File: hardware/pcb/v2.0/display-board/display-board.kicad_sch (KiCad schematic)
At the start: 53 parts, among them J1 Conn_01x01_Socket, J2 Conn_01x01_Socket, J3 Conn_01x01_Socket, J4 Conn_01x01_Socket, J5 Conn_01x01_Socket, J6 Conn_01x01_Socket, Q1 AO3400A, Q2 AO3401A, Q3 AO3400A, Q4 AO3401A, Q5 AO3400A, Q6 AO3401A, Q7 AO3400A, SW1 SW_Push, SW2 SW_Push, U1 TLC5940PWP, U2 7Seg 2Dig 0.56in, U3 GS-S2011AB, U4 7Seg 2Dig 0.56in, U5 GS-S2011AB

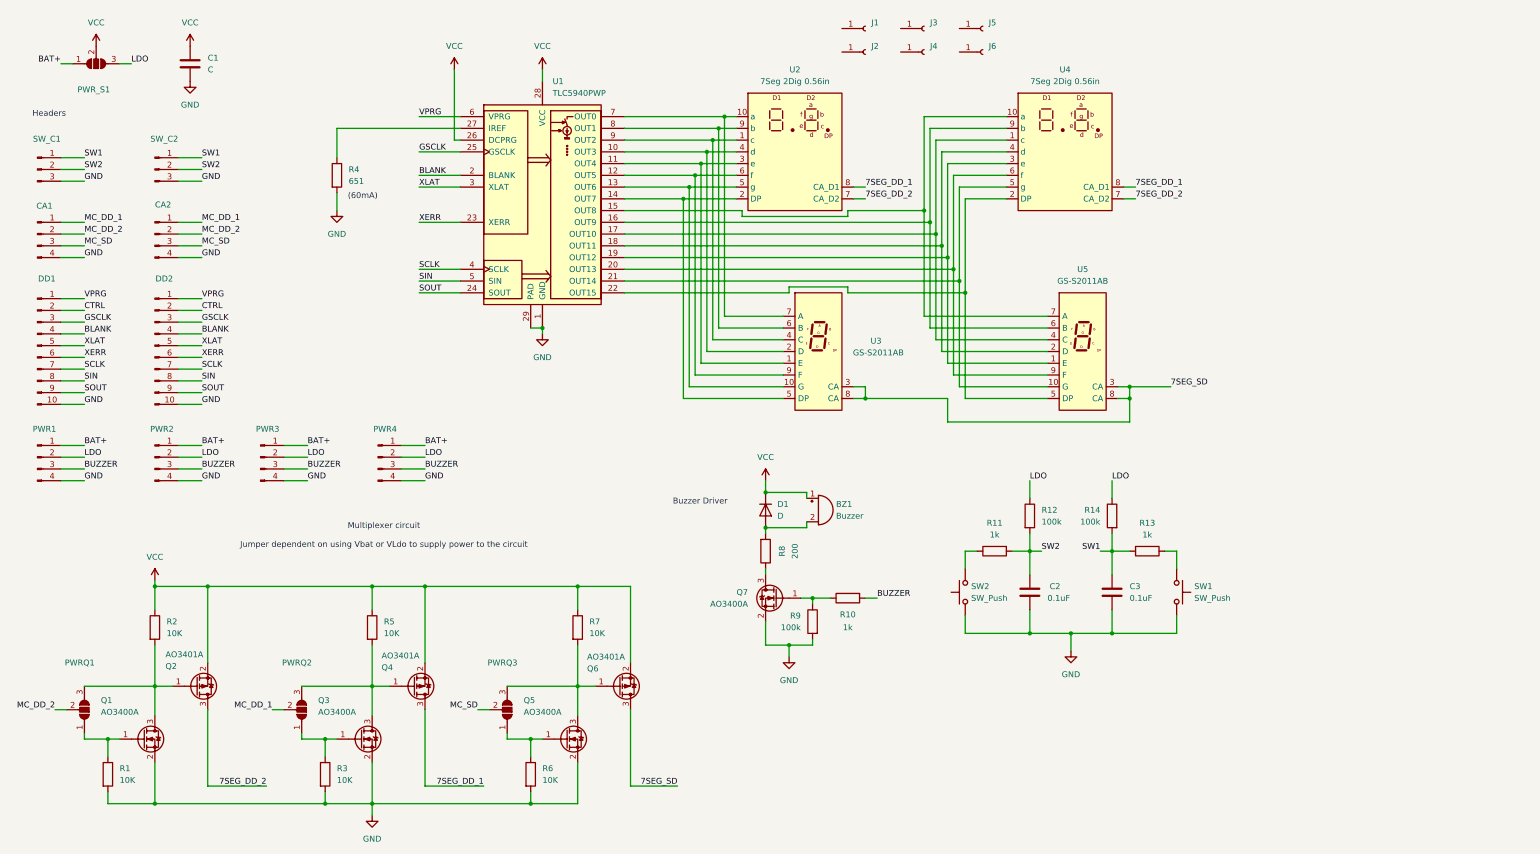
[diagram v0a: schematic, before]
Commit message: v2.0 of the main and display board is ready and in production
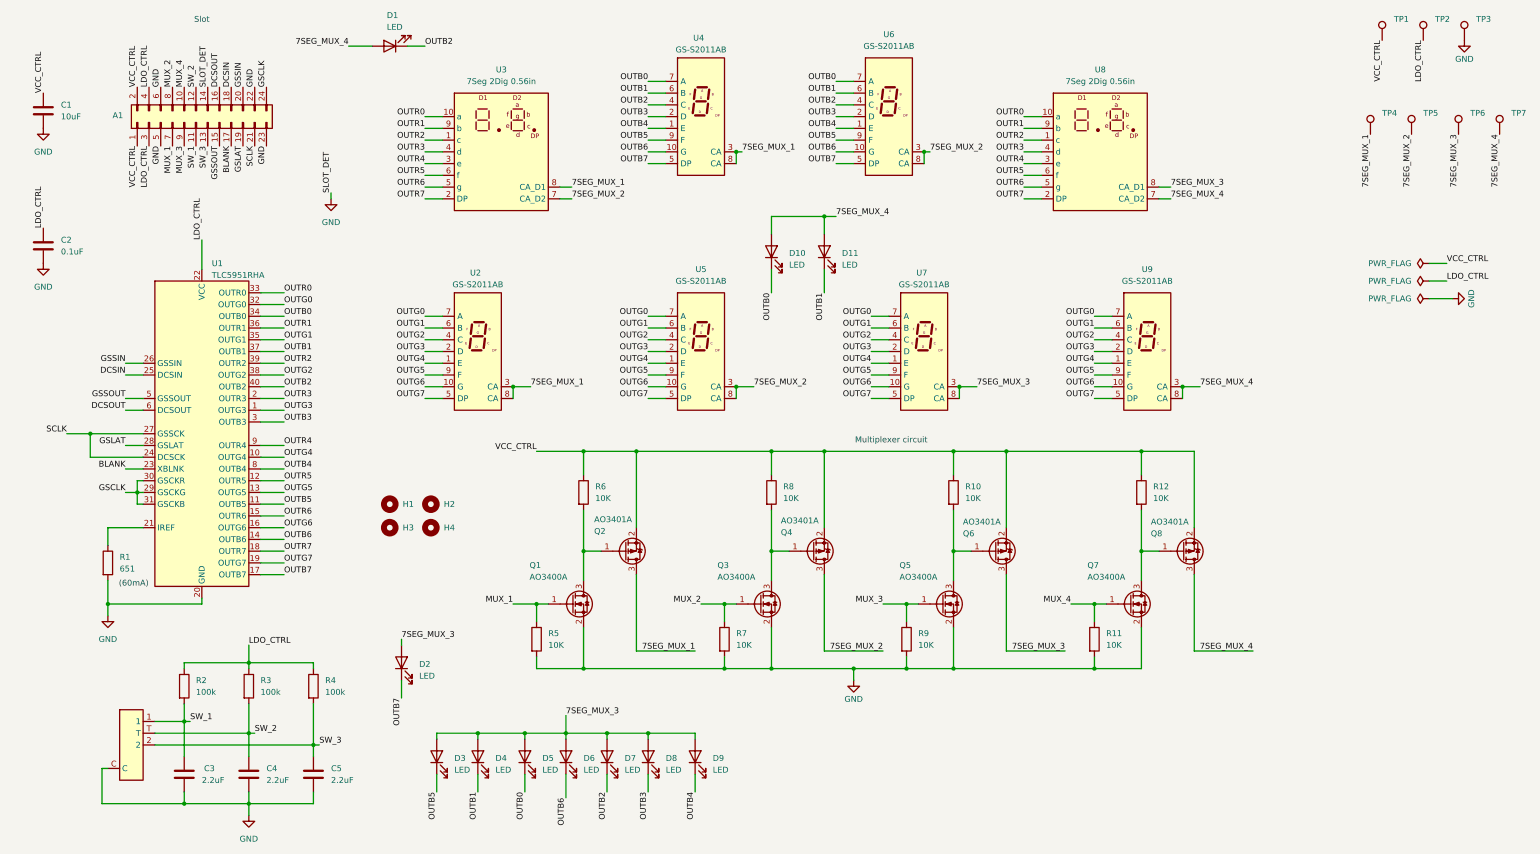
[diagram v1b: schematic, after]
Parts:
- removed BZ1: Buzzer, Buzzer_Beeper:Buzzer_TDK_PS1240P02BT_D12.2mm_H6.5mm, symbol Device:Buzzer
- removed CA1, CA2, PWR1, PWR2, PWR3, PWR4: Conn_01x04_Pin, Connector_PinHeader_1.27mm:PinHeader_1x04_P1.27mm_Vertical, symbol Connector:Conn_01x04_Pin
- removed D1: D, Diode_SMD:D_SOD-323_HandSoldering, symbol Device:D
- removed DD1, DD2: Conn_01x10_Pin, Connector_PinSocket_1.27mm:PinSocket_1x10_P1.27mm_Vertical, symbol Connector:Conn_01x10_Pin
- removed J1, J2, J3, J4, J5, J6: Conn_01x01_Socket, MountingHole:MountingHole_2mm, symbol Connector:Conn_01x01_Socket
- removed PWRQ1, PWRQ2, PWRQ3, PWR_S1: SolderJumper_3_Open, Jumper:SolderJumper-3_P1.3mm_Open_RoundedPad1.0x1.5mm_NumberLabels, symbol Jumper:SolderJumper_3_Open
- removed R10, R13: 1k, Resistor_SMD:R_0603_1608Metric_Pad0.98x0.95mm_HandSolder, symbol Device:R
- removed R8: 200, Resistor_SMD:R_0603_1608Metric_Pad0.98x0.95mm_HandSolder, symbol Device:R
- removed R9: 100k, Resistor_SMD:R_0603_1608Metric_Pad0.98x0.95mm_HandSolder, symbol Device:R
- removed SW1, SW2: SW_Push, Luis:Button_12x12x7.3, symbol Switch:SW_Push
- removed SW_C1, SW_C2: Conn_01x03_Pin, Connector_PinHeader_1.27mm:PinHeader_1x03_P1.27mm_Vertical, symbol Connector:Conn_01x03_Pin
- removed U1: TLC5940PWP, Package_SO:HTSSOP-28-1EP_4.4x9.7mm_P0.65mm_EP3.4x9.5mm_Mask2.4x6.17mm_ThermalVias, symbol Driver_LED:TLC5940PWP
- added A1: Conn_02x12_Odd_Even, Connector_PinHeader_1.27mm:PinHeader_2x12_P1.27mm_Vertical_SMD, symbol Connector_Generic:Conn_02x12_Odd_Even
- added C2: 0.1uF, Capacitor_SMD:C_0603_1608Metric_Pad1.08x0.95mm_HandSolder, symbol Device:C
- added C5: 2.2uF, Capacitor_SMD:C_0805_2012Metric_Pad1.18x1.45mm_HandSolder, symbol Device:C
- added D1: LED, Luis:LED Bar, symbol Device:LED
- added D10, D11: LED, LED_SMD:LED_0603_1608Metric_Pad1.05x0.95mm_HandSolder, symbol Device:LED
- added D2, D3, D4, D5, D6, D7, D8, D9: LED, LED_SMD:LED_0805_2012Metric_Pad1.15x1.40mm_HandSolder, symbol Device:LED
- added H1, H2, H3, H4: MountingHole, MountingHole:MountingHole_2mm, symbol Mechanical:MountingHole
- added Q8: AO3401A, Package_TO_SOT_SMD:SOT-23, symbol Transistor_FET:AO3401A
- added R1: 651, Resistor_SMD:R_0603_1608Metric_Pad0.98x0.95mm_HandSolder, symbol Device:R
- added R12: 10K, Resistor_SMD:R_0603_1608Metric_Pad0.98x0.95mm_HandSolder, symbol Device:R
- added SW1: ~, Luis:Thumbwheel, symbol Luis:Thumbwheel
- added TP1, TP2, TP3, TP4, TP5, TP6, TP7: TestPoint, TestPoint:TestPoint_Pad_D1.0mm, symbol Connector:TestPoint
- added U1: TLC5951RHA, Package_DFN_QFN:Texas_RHA0040B_VQFN-40-1EP_6x6mm_P0.5mm_EP4.15x4.15mm_ThermalVias, symbol Driver_LED:TLC5951RHA
- added U2, U5, U7, U9: GS-S2011AB, Luis:GS-2011AB, symbol Luis:7Seg 0.2in
- C1: value C -> 10uF
- C3: renamed from C2; value 0.1uF -> 2.2uF
- C4: renamed from C3; value 0.1uF -> 2.2uF
- R11: value 1k -> 10K
- R4: value 651 -> 100k
- renumbered R7 to R10, R12 to R2, R14 to R3, R1 to R5, R2 to R6, R3 to R7, R5 to R8, R6 to R9, U2 to U3, U3 to U4, U5 to U6, U4 to U8
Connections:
- net LDO is gone; now on net LDO_CTRL: R2.1, R3.1
- net BLANK: now also A1.17 (Pin_17), U1.23 (XBLNK)
- net GND: now also R11.2, A1.14 (Pin_14), A1.22 (Pin_22), A1.23 (Pin_23), A1.5 (Pin_5), A1.6 (Pin_6), C2.2, C5.2, R1.2, SW1.C, TP3.1, U1.20 (GND), U1.41 (GND); no longer R4.2
- net GSCLK: now also A1.24 (Pin_24), U1.29 (GSCKG), U1.30 (GSCKR), U1.31 (GSCKB)
- net SCLK: now also A1.21 (Pin_21), U1.24 (DCSCK), U1.27 (GSSCK)
- net MUX_3: now reaches Q5.1 (G), R9.1
- net MUX_3: now also A1.9 (Pin_9)
- net OUTB3: now reaches U4.2 (D)
- net OUTB3: now also U6.2 (D), D8.1 (K), U1.3 (OUTB3); no longer U3.4 (d)
- net OUTB4: now reaches U4.1 (E)
- net OUTB4: now also U6.1 (E), D9.1 (K), U1.8 (OUTB4); no longer U3.3 (e)
- net OUTB5: now reaches U4.9 (F)
- net OUTB5: now also U6.9 (F), D3.1 (K), U1.11 (OUTB5); no longer U3.6 (f)
- net OUTB6: now reaches U4.10 (G)
- net OUTB6: now also U6.10 (G), D6.1 (K), U1.14 (OUTB6); no longer U3.5 (g)
- net OUTB7: now reaches U4.5 (DP)
- net OUTB7: now also U6.5 (DP), D2.1 (K), U1.17 (OUTB7); no longer U3.2 (DP)
- net OUTB0: now reaches U6.7 (A)
- net OUTB0: now also U4.7 (A), D10.1 (K), D5.1 (K), U1.34 (OUTB0); no longer U8.10 (a)
- net OUTB1: now reaches U6.6 (B)
- net OUTB1: now also U4.6 (B), D11.1 (K), D4.1 (K), U1.37 (OUTB1); no longer U8.9 (b)
- net OUTB2: now reaches U6.4 (C)
- net OUTB2: now also U4.4 (C), D1.1 (K), D7.1 (K), U1.40 (OUTB2); no longer U8.1 (c)
- net OUTR3: now reaches U8.4 (d)
- net OUTR3: now also U3.4 (d), U1.2 (OUTR3); no longer U6.2 (D)
- net OUTR4: now reaches U8.3 (e)
- net OUTR4: now also U3.3 (e), U1.9 (OUTR4); no longer U6.1 (E)
- net OUTR5: now reaches U8.6 (f)
- net OUTR5: now also U3.6 (f), U1.12 (OUTR5); no longer U6.9 (F)
- net OUTR6: now reaches U8.5 (g)
- net OUTR6: now also U3.5 (g), U1.15 (OUTR6); no longer U6.10 (G)
- net OUTR7: now reaches U8.2 (DP)
- net OUTR7: now also U3.2 (DP), U1.18 (OUTR7); no longer U6.5 (DP)
- net LDO_CTRL: now reaches R4.1
- net LDO_CTRL: now also A1.3 (Pin_3), A1.4 (Pin_4), C2.1, TP2.1, U1.22 (VCC)
- net OUTR0: now reaches U3.10 (a)
- net OUTR0: now also U8.10 (a), U1.33 (OUTR0); no longer U4.7 (A)
- net OUTR1: now reaches U3.9 (b)
- net OUTR1: now also U8.9 (b), U1.36 (OUTR1); no longer U4.6 (B)
- net OUTR2: now reaches U3.1 (c)
- net OUTR2: now also U8.1 (c), U1.39 (OUTR2); no longer U4.4 (C)
- net MUX_4: now reaches Q7.1 (G)
- net MUX_4: now also R11.1, A1.10 (Pin_10)
- net MUX_1: now reaches Q1.1 (G), R5.1
- net MUX_1: now also A1.7 (Pin_7)
- net MUX_2: now reaches Q3.1 (G), R7.1
- net MUX_2: now also A1.8 (Pin_8)
- net at Q7.3 (D): now also Q8.1 (G), R12.2
- removed net 7SEG_DD_1: Q4.3 (D), U3.8 (CA_D1), U8.8 (CA_D1)
- removed net 7SEG_DD_2: Q2.3 (D), U3.7 (CA_D2), U8.7 (CA_D2)
- removed net 7SEG_SD: Q6.3 (D), U4.3 (CA), U4.8 (CA), U6.3 (CA), U6.8 (CA)
- net SW1 renamed SW_2
- net SW_2: now also A1.12 (Pin_12), SW1.T
- net SW2 renamed SW_1
- net SW_1: now also A1.11 (Pin_11), SW1.1; no longer R11.2
- net VCC renamed VCC_CTRL
- net VCC_CTRL: now also A1.1 (Pin_1), A1.2 (Pin_2), Q8.2 (S), R12.1, TP1.1
- new net: R1.1, U1.21 (IREF)
- new net 7SEG_MUX_1: Q2.3 (D), TP4.1, U2.3 (CA), U2.8 (CA), U3.8 (CA_D1), U4.3 (CA), U4.8 (CA)
- new net 7SEG_MUX_2: Q4.3 (D), TP5.1, U3.7 (CA_D2), U5.3 (CA), U5.8 (CA), U6.3 (CA), U6.8 (CA)
- new net 7SEG_MUX_3: D2.2 (A), D3.2 (A), D4.2 (A), D5.2 (A), D6.2 (A), D7.2 (A), D8.2 (A), D9.2 (A), Q6.3 (D), TP6.1, U7.3 (CA), U7.8 (CA), U8.8 (CA_D1)
- new net 7SEG_MUX_4: D1.2 (A), D10.2 (A), D11.2 (A), Q8.3 (D), TP7.1, U8.7 (CA_D2), U9.3 (CA), U9.8 (CA)
- new net DCSIN: A1.18 (Pin_18), U1.25 (DCSIN)
- new net DCSOUT: A1.16 (Pin_16), U1.6 (DCSOUT)
- new net GSLAT: A1.19 (Pin_19), U1.28 (GSLAT)
- new net GSSIN: A1.20 (Pin_20), U1.26 (GSSIN)
- new net GSSOUT: A1.15 (Pin_15), U1.5 (GSSOUT)
- new net OUTG0: U1.32 (OUTG0), U2.7 (A), U5.7 (A), U7.7 (A), U9.7 (A)
- new net OUTG1: U1.35 (OUTG1), U2.6 (B), U5.6 (B), U7.6 (B), U9.6 (B)
- new net OUTG2: U1.38 (OUTG2), U2.4 (C), U5.4 (C), U7.4 (C), U9.4 (C)
- new net OUTG3: U1.1 (OUTG3), U2.2 (D), U5.2 (D), U7.2 (D), U9.2 (D)
- new net OUTG4: U1.10 (OUTG4), U2.1 (E), U5.1 (E), U7.1 (E), U9.1 (E)
- new net OUTG5: U1.13 (OUTG5), U2.9 (F), U5.9 (F), U7.9 (F), U9.9 (F)
- new net OUTG6: U1.16 (OUTG6), U2.10 (G), U5.10 (G), U7.10 (G), U9.10 (G)
- new net OUTG7: U1.19 (OUTG7), U2.5 (DP), U5.5 (DP), U7.5 (DP), U9.5 (DP)
- new net SW_3: A1.13 (Pin_13), C5.1, R4.2, SW1.2
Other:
- note added: "Multiplexer circuit"
- note added: "Slot"
- note removed: "Buzzer Driver"
- note removed: "Headers"
- note removed: "Multiplexer circuit Jumper dependent on using Vbat or VLdo to supply power to the circuit"
- moved on the sheet: C1, C3, C4, Q1, Q2, Q3, Q4, Q5, Q6, R10, R2, R3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

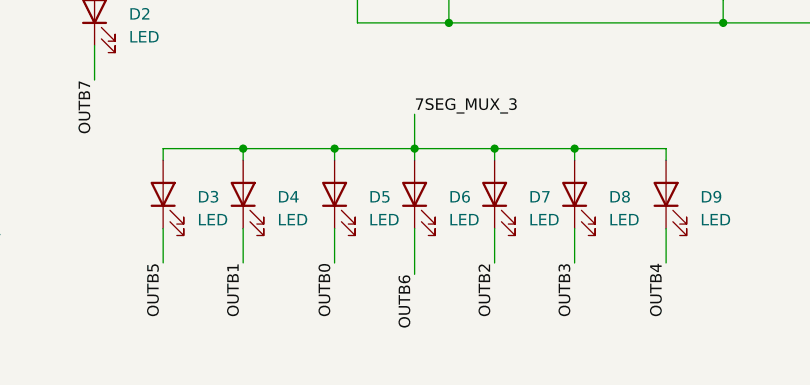
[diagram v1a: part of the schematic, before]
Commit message: new version in the works, time is not yet functional but the new board is very much working
ds3231 vbat is switched with the vcc - fixed
have to fix capacitor resonance since it is really annoying
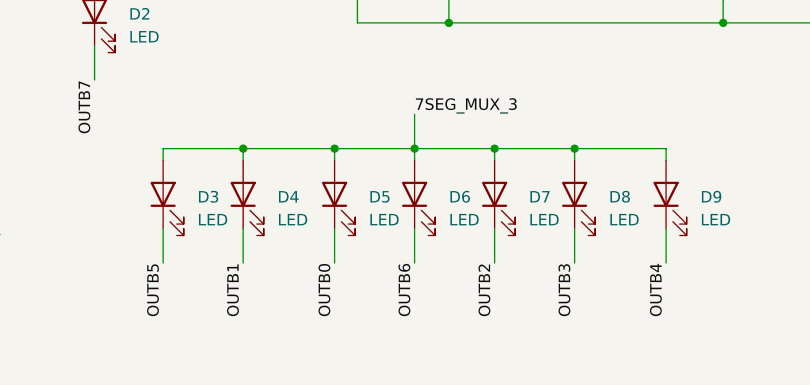
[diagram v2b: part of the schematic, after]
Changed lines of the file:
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@@
 	(wire
 		(pts
-			(xy 134.62 180.34) (xy 134.62 185.42)
+			(xy 134.62 180.34) (xy 134.62 184.15)
 		)
 		(stroke
@@
 	)
 	(label "OUTB6"
-		(at 134.62 185.42 270)
+		(at 134.62 184.15 270)
 		(effects
 			(font
